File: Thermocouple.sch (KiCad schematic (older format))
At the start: 28 parts, among them P2 CONN_3X2, P3 CONN_2, U2 MCP3901, U3 LMT84, U4 OPA4170

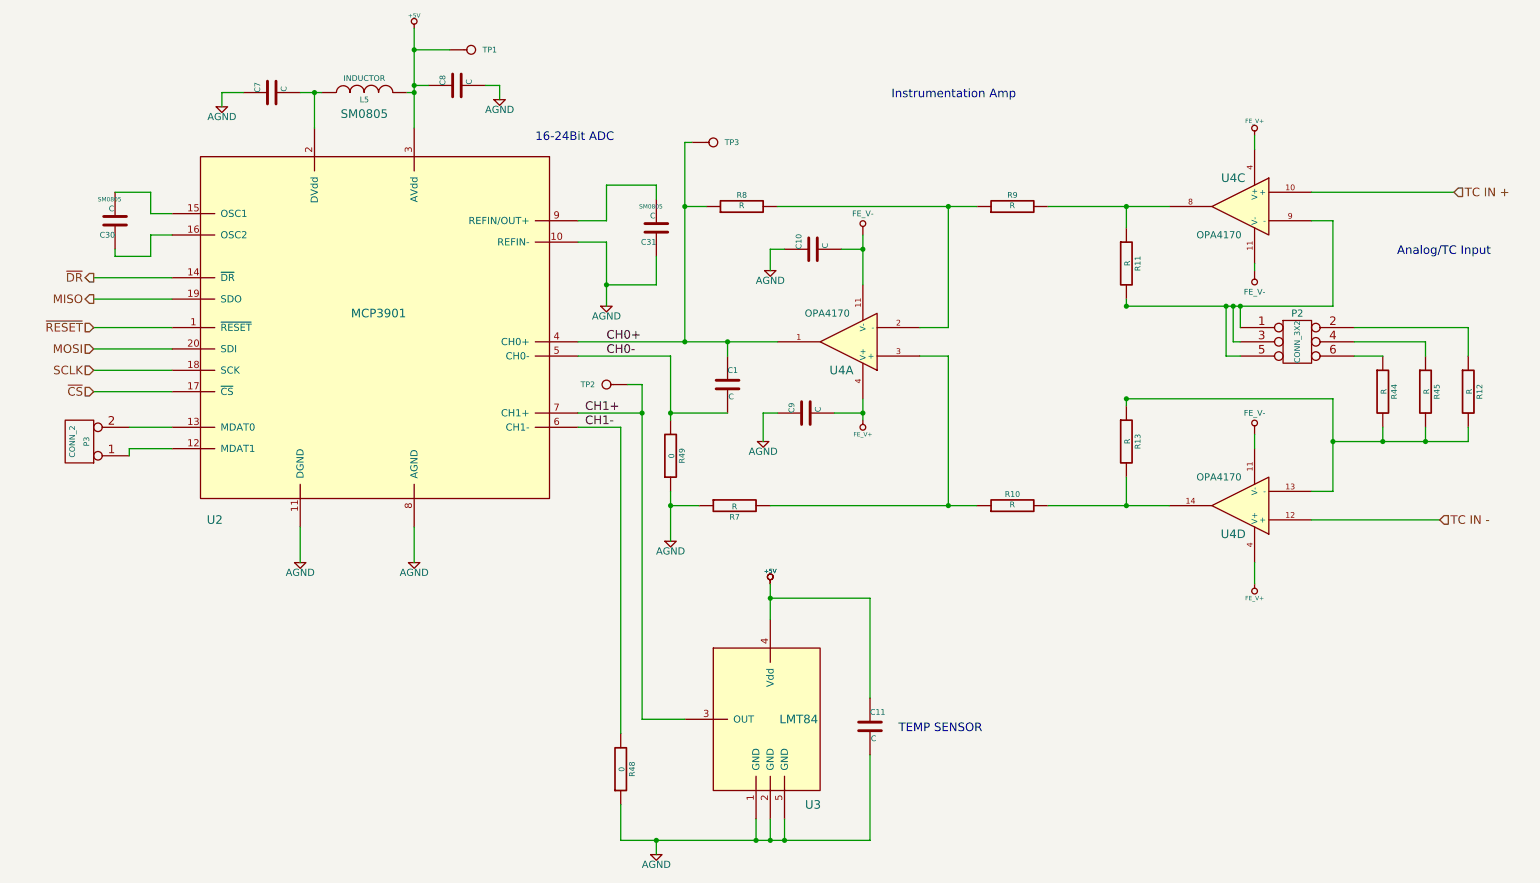
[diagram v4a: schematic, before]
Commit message: Analog IO Cleanup/Additions
Added some placed holder caps and resistors
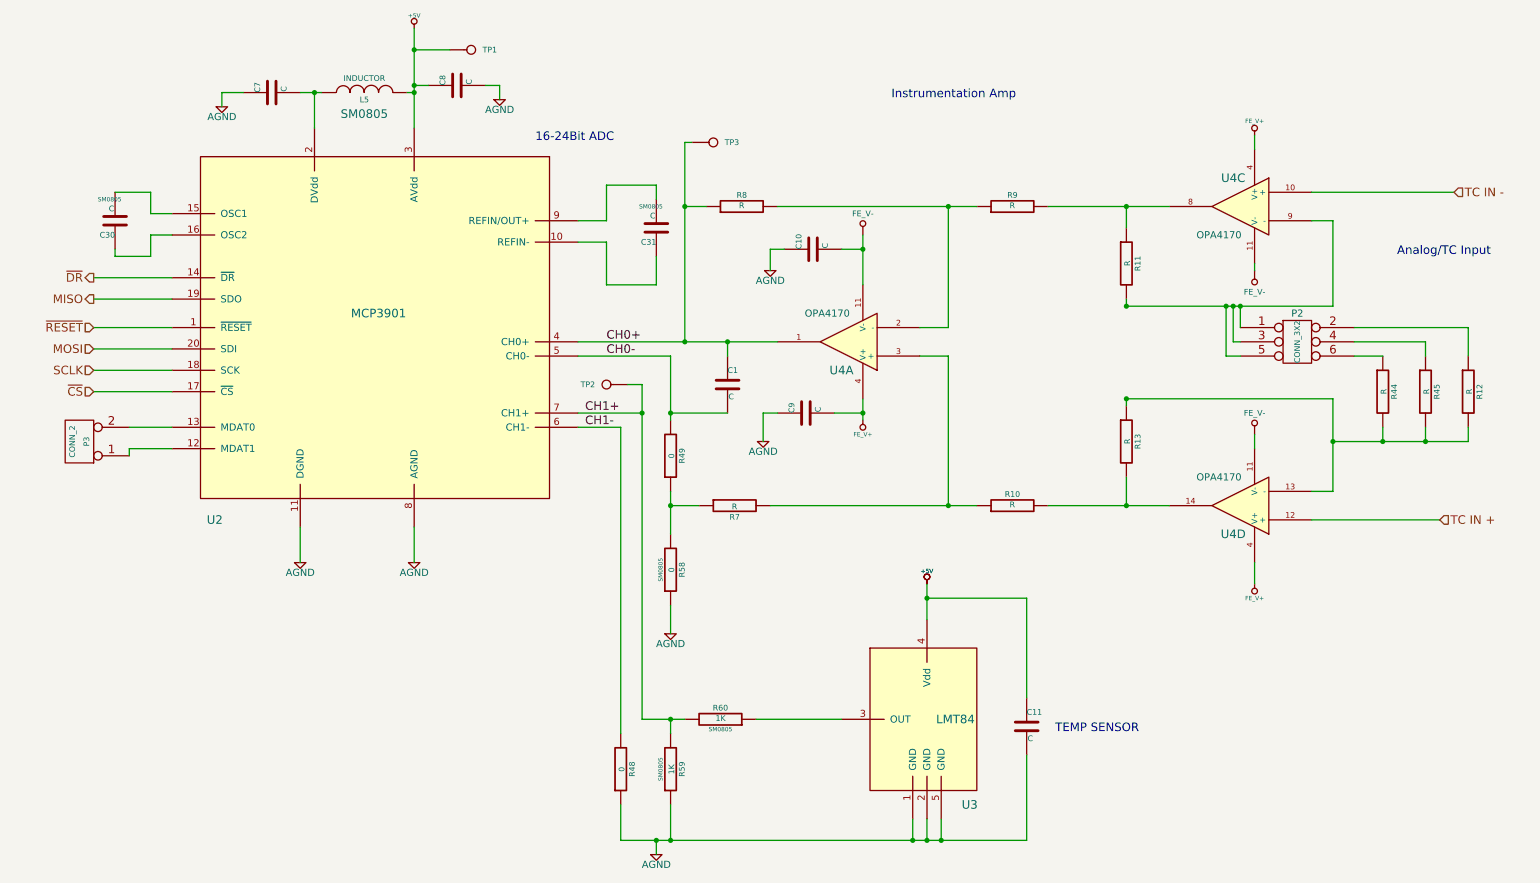
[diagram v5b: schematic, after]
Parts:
- added R58: 0, SM0805, symbol R
- added R59, R60: 1K, SM0805, symbol R
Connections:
- net AGND: now also R58.1, R59.1; no longer C31.1, R49.1, R7.1, U2.10 (REFIN-)
- net CH1+: now also R59.2, R60.2; no longer U3.3 (OUT)
- net TC IN +: now also U4.12 (+); no longer U4.10 (+)
- net TC IN -: now also U4.10 (+); no longer U4.12 (+)
- new net: R49.1, R58.2, R7.1
- new net: C31.1, U2.10 (REFIN-)
- new net: R60.1, U3.3 (OUT)
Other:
- moved on the sheet: C11, U3
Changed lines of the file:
@@
-EESchema Schematic File Version 2  date 12/18/2013 11:27:15 PM
+EESchema Schematic File Version 2  date 2/16/2014 3:41:32 PM
 LIBS:power
 LIBS:device
@@
 Sheet 2 9
 Title ""
-Date "19 dec 2013"
+Date "16 feb 2014"
 Rev ""
 Comp ""
@@
 $EndDescr
 Text HLabel 10400 2250 2    60   Input ~ 0
+TC IN -
+Text HLabel 10300 4550 2    60   Input ~ 0
 TC IN +
-Text HLabel 10300 4550 2    60   Input ~ 0
-TC IN -
 Text HLabel 850  3350 0    60   Input ~ 0
 MOSI
@@
 L LMT84 U3
 U 1 1 52579673
-P 5600 6100
-F 0 "U3" H 5900 5650 60  0000 C CNN
-F 1 "LMT84" H 5800 6250 60  0000 C CNN
-F 2 "" H 5700 6100 60  0000 C CNN
-F 3 "" H 5700 6100 60  0000 C CNN
-	1    5600 6100
-	1    0    0    -1
-$EndComp
-Wire Wire Line
-	4700 5950 5000 5950
+P 6700 6100
+F 0 "U3" H 7000 5650 60  0000 C CNN
+F 1 "LMT84" H 6900 6250 60  0000 C CNN
+F 2 "" H 6800 6100 60  0000 C CNN
+F 3 "" H 6800 6100 60  0000 C CNN
+	1    6700 6100
+	1    0    0    -1
+$EndComp
 Wire Wire Line
 	4700 3600 4700 5950
@@
 	4250 3900 4550 3900
 Wire Wire Line
-	4550 6800 6300 6800
-Wire Wire Line
-	5500 6800 5500 6650
-Wire Wire Line
-	5600 6800 5600 6650
-Connection ~ 5500 6800
-Wire Wire Line
-	5700 6800 5700 6650
-Connection ~ 5600 6800
+	4550 6800 7400 6800
+Wire Wire Line
+	6600 6800 6600 6650
+Wire Wire Line
+	6700 6800 6700 6650
+Connection ~ 6600 6800
+Wire Wire Line
+	6800 6800 6800 6650
+Connection ~ 6700 6800
 Wire Wire Line
 	4800 6900 4800 6800
 Connection ~ 4800 6800
 $Comp
-L +5V #PWR11
+L +5V #PWR01
 U 1 1 5257A1D1
-P 5600 5000
-F 0 "#PWR11" H 5600 5090 20  0001 C CNN
-F 1 "+5V" H 5600 5090 30  0000 C CNN
-F 2 "~" H 5600 5000 60  0000 C CNN
-F 3 "~" H 5600 5000 60  0000 C CNN
-	1    5600 5000
-	1    0    0    -1
-$EndComp
-Wire Wire Line
-	5600 5000 5600 5250
+P 6700 5000
+F 0 "#PWR01" H 6700 5090 20  0001 C CNN
+F 1 "+5V" H 6700 5090 30  0000 C CNN
+F 2 "~" H 6700 5000 60  0000 C CNN
+F 3 "~" H 6700 5000 60  0000 C CNN
+	1    6700 5000
+	1    0    0    -1
+$EndComp
+Wire Wire Line
+	6700 5000 6700 5250
 $Comp
 L C C11
 U 1 1 5257A1D8
-P 6300 6000
-F 0 "C11" H 6300 6100 40  0000 L CNN
-F 1 "C" H 6306 5915 40  0000 L CNN
-F 2 "~" H 6338 5850 30  0000 C CNN
-F 3 "~" H 6300 6000 60  0000 C CNN
-	1    6300 6000
-	1    0    0    -1
-$EndComp
-Wire Wire Line
-	6300 5800 6300 5100
-Wire Wire Line
-	6300 5100 5600 5100
-Connection ~ 5600 5100
-Wire Wire Line
-	6300 6800 6300 6200
-Connection ~ 5700 6800
+P 7400 6000
+F 0 "C11" H 7400 6100 40  0000 L CNN
+F 1 "C" H 7406 5915 40  0000 L CNN
+F 2 "~" H 7438 5850 30  0000 C CNN
+F 3 "~" H 7400 6000 60  0000 C CNN
+	1    7400 6000
+	1    0    0    -1
+$EndComp
+Wire Wire Line
+	7400 5800 7400 5100
+Wire Wire Line
+	7400 5100 6700 5100
+Connection ~ 6700 5100
+Wire Wire Line
+	7400 6800 7400 6200
+Connection ~ 6800 6800
 $Comp
 L C C9
@@
 	6050 3800 6250 3800
 $Comp
-L +5V #PWR12
+L +5V #PWR02
 U 1 1 5257A5A4
-P 5600 5000
-F 0 "#PWR12" H 5600 5090 20  0001 C CNN
-F 1 "+5V" H 5600 5090 30  0000 C CNN
-F 2 "~" H 5600 5000 60  0000 C CNN
-F 3 "~" H 5600 5000 60  0000 C CNN
-	1    5600 5000
-	1    0    0    -1
-$EndComp
-$Comp
-L +5V #PWR3
+P 6700 5000
+F 0 "#PWR02" H 6700 5090 20  0001 C CNN
+F 1 "+5V" H 6700 5090 30  0000 C CNN
+F 2 "~" H 6700 5000 60  0000 C CNN
+F 3 "~" H 6700 5000 60  0000 C CNN
+	1    6700 5000
+	1    0    0    -1
+$EndComp
+$Comp
+L +5V #PWR03
 U 1 1 5257A5AA
 P 3100 1100
-F 0 "#PWR3" H 3100 1190 20  0001 C CNN
+F 0 "#PWR03" H 3100 1190 20  0001 C CNN
 F 1 "+5V" H 3100 1190 30  0000 C CNN
 F 2 "~" H 3100 1100 60  0000 C CNN
@@
 Wire Wire Line
 	3100 4600 3100 4850
-Text Notes 6500 6050 0    60   ~ 0
+Text Notes 7600 6050 0    60   ~ 0
 TEMP SENSOR
 Text HLabel 850  3200 0    60   Input ~ 0
@@
 $EndComp
 Wire Wire Line
-	4900 4350 4900 4700
+	4900 4350 4900 4650
 $Comp
 L R R48
@@
 	4550 3900 4550 6050
 $Comp
-L FE_V- #PWR13
+L FE_V- #PWR11
 U 1 1 526E01DB
 P 6250 2550
-F 0 "#PWR13" H 6250 2750 40  0001 C CNN
+F 0 "#PWR11" H 6250 2750 40  0001 C CNN
 F 1 "FE_V-" H 6250 2700 40  0000 C CNN
 F 2 "~" H 6250 2550 60  0000 C CNN
@@
 $EndComp
 $Comp
-L FE_V+ #PWR14
+L FE_V+ #PWR04
 U 1 1 526E01E1
 P 6250 3850
-F 0 "#PWR14" H 6250 3950 30  0001 C CNN
+F 0 "#PWR04" H 6250 3950 30  0001 C CNN
 F 1 "FE_V+" H 6250 3950 30  0000 C CNN
 F 2 "~" H 6250 3850 60  0000 C CNN
@@
 $EndComp
 $Comp
-L FE_V+ #PWR18
+L FE_V+ #PWR05
 U 1 1 526E01F1
 P 9000 5000
-F 0 "#PWR18" H 9000 5100 30  0001 C CNN
+F 0 "#PWR05" H 9000 5100 30  0001 C CNN
 F 1 "FE_V+" H 9000 5100 30  0000 C CNN
 F 2 "~" H 9000 5000 60  0000 C CNN
@@
 $EndComp
 $Comp
-L FE_V+ #PWR15
+L FE_V+ #PWR06
 U 1 1 526E020D
 P 9000 1850
-F 0 "#PWR15" H 9000 1950 30  0001 C CNN
+F 0 "#PWR06" H 9000 1950 30  0001 C CNN
 F 1 "FE_V+" H 9000 1950 30  0000 C CNN
 F 2 "~" H 9000 1850 60  0000 C CNN
@@
 $EndComp
 $Comp
-L AGND #PWR4
+L AGND #PWR07
 U 1 1 527EEF67
 P 3100 4850
-F 0 "#PWR4" H 3100 4850 40  0001 C CNN
+F 0 "#PWR07" H 3100 4850 40  0001 C CNN
 F 1 "AGND" H 3100 4780 50  0000 C CNN
 F 2 "~" H 3100 4850 60  0000 C CNN
@@
 $EndComp
 $Comp
-L AGND #PWR2
+L AGND #PWR08
 U 1 1 527EEF6D
 P 2300 4850
-F 0 "#PWR2" H 2300 4850 40  0001 C CNN
+F 0 "#PWR08" H 2300 4850 40  0001 C CNN
 F 1 "AGND" H 2300 4780 50  0000 C CNN
 F 2 "~" H 2300 4850 60  0000 C CNN
@@
 $EndComp
 $Comp
-L AGND #PWR1
+L AGND #PWR09
 U 1 1 527EEF73
 P 1750 1650
-F 0 "#PWR1" H 1750 1650 40  0001 C CNN
+F 0 "#PWR09" H 1750 1650 40  0001 C CNN
 F 1 "AGND" H 1750 1580 50  0000 C CNN
 F 2 "~" H 1750 1650 60  0000 C CNN
@@
 $EndComp
 $Comp
-L AGND #PWR5
+L AGND #PWR010
 U 1 1 527EEF79
 P 3700 1600
-F 0 "#PWR5" H 3700 1600 40  0001 C CNN
+F 0 "#PWR010" H 3700 1600 40  0001 C CNN
 F 1 "AGND" H 3700 1530 50  0000 C CNN
 F 2 "~" H 3700 1600 60  0000 C CNN
@@
 $EndComp
 $Comp
-L AGND #PWR10
+L AGND #PWR011
 U 1 1 527EEF7F
 P 5600 2800
-F 0 "#PWR10" H 5600 2800 40  0001 C CNN
+F 0 "#PWR011" H 5600 2800 40  0001 C CNN
 F 1 "AGND" H 5600 2730 50  0000 C CNN
 F 2 "~" H 5600 2800 60  0000 C CNN
@@
 $EndComp
 $Comp
-L AGND #PWR9
+L AGND #PWR012
 U 1 1 527EEF85
 P 5550 4000
-F 0 "#PWR9" H 5550 4000 40  0001 C CNN
+F 0 "#PWR012" H 5550 4000 40  0001 C CNN
 F 1 "AGND" H 5550 3930 50  0000 C CNN
 F 2 "~" H 5550 4000 60  0000 C CNN
@@
 $EndComp
 $Comp
-L AGND #PWR8
+L AGND #PWR013
 U 1 1 527EEF8B
-P 4900 4700
-F 0 "#PWR8" H 4900 4700 40  0001 C CNN
-F 1 "AGND" H 4900 4630 50  0000 C CNN
-F 2 "~" H 4900 4700 60  0000 C CNN
-F 3 "~" H 4900 4700 60  0000 C CNN
-	1    4900 4700
-	1    0    0    -1
-$EndComp
-$Comp
-L AGND #PWR7
+P 4900 5350
+F 0 "#PWR013" H 4900 5350 40  0001 C CNN
+F 1 "AGND" H 4900 5280 50  0000 C CNN
+F 2 "~" H 4900 5350 60  0000 C CNN
+F 3 "~" H 4900 5350 60  0000 C CNN
+	1    4900 5350
+	1    0    0    -1
+$EndComp
+$Comp
+L AGND #PWR014
 U 1 1 527EEF91
 P 4800 6900
-F 0 "#PWR7" H 4800 6900 40  0001 C CNN
+F 0 "#PWR014" H 4800 6900 40  0001 C CNN
 F 1 "AGND" H 4800 6830 50  0000 C CNN
 F 2 "~" H 4800 6900 60  0000 C CNN
@@
 	4450 2200 4450 2450
 Wire Wire Line
-	4450 2600 4450 3050
-Wire Wire Line
 	4450 2900 4800 2900
 Wire Wire Line
 	4800 2900 4800 2700
-$Comp
-L AGND #PWR6
-U 1 1 529271FF
-P 4450 3050
-F 0 "#PWR6" H 4450 3050 40  0001 C CNN
-F 1 "AGND" H 4450 2980 50  0000 C CNN
-F 2 "~" H 4450 3050 60  0000 C CNN
-F 3 "~" H 4450 3050 60  0000 C CNN
-	1    4450 3050
-	1    0    0    -1
-$EndComp
-Connection ~ 4450 2900
 $Comp
 L CONN_1 TP3
@@
 	3100 1250 3350 1250
 Connection ~ 3100 1250
+$Comp
+L R R58
+U 1 1 53010C4F
+P 4900 4900
+F 0 "R58" V 4980 4900 40  0000 C CNN
+F 1 "0" V 4907 4901 40  0000 C CNN
+F 2 "SM0805" V 4830 4900 30  0000 C CNN
+F 3 "~" H 4900 4900 30  0000 C CNN
+	1    4900 4900
+	1    0    0    1
+$EndComp
+Wire Wire Line
+	4900 5150 4900 5350
+$Comp
+L R R60
+U 1 1 53010D95
+P 5250 5950
+F 0 "R60" V 5330 5950 40  0000 C CNN
+F 1 "1K" V 5257 5951 40  0000 C CNN
+F 2 "SM0805" V 5180 5950 30  0000 C CNN
+F 3 "~" H 5250 5950 30  0000 C CNN
+	1    5250 5950
+	0    1    -1   0
+$EndComp
+Wire Wire Line
+	6100 5950 5500 5950
+Wire Wire Line
+	4700 5950 5000 5950
+$Comp
+L R R59
+U 1 1 53010EB2
+P 4900 6300
+F 0 "R59" V 4980 6300 40  0000 C CNN
+F 1 "1K" V 4907 6301 40  0000 C CNN
+F 2 "SM0805" V 4830 6300 30  0000 C CNN
+F 3 "~" H 4900 6300 30  0000 C CNN
+	1    4900 6300
+	1    0    0    1
+$EndComp
+Wire Wire Line
+	4900 5950 4900 6050
+Connection ~ 4900 5950
+Wire Wire Line
+	4900 6550 4900 6800
+Connection ~ 4900 6800
+Wire Wire Line
+	4450 2600 4450 2900
 $EndSCHEMATC

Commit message: Added Passive Values and SPICE models
As part of week 1 of Session 1B, we added a SPICE model of the In amp
and went through and assigned values to all of the passive components.
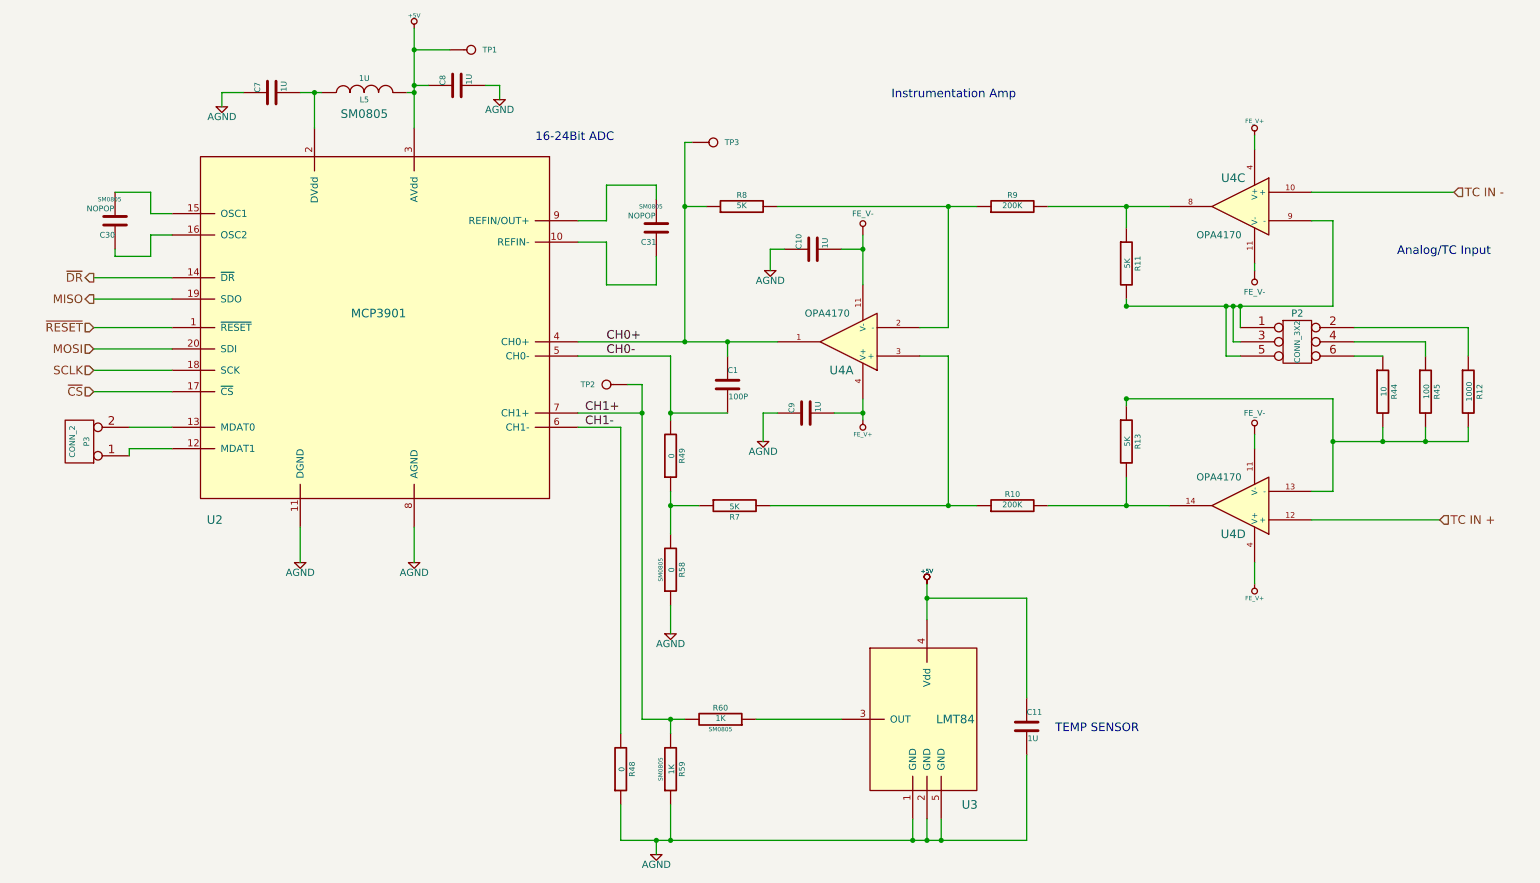
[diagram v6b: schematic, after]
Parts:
- C1: value C -> 100P
- C10, C11, C7, C8, C9: value C -> 1U
- C30, C31: value C -> NOPOP
- L5: value INDUCTOR -> 1U
- R10, R9: value R -> 200K
- R11, R13, R7, R8: value R -> 5K
- R12: value R -> 1000
- R44: value R -> 10
- R45: value R -> 100
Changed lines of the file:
@@
-EESchema Schematic File Version 2  date 2/16/2014 3:41:32 PM
+EESchema Schematic File Version 2  date 4/16/2014 11:04:06 PM
 LIBS:power
 LIBS:device
@@
 Sheet 2 9
 Title ""
-Date "16 feb 2014"
+Date "17 apr 2014"
 Rev ""
 Comp ""
@@
 P 5300 3600
 F 0 "C1" H 5300 3700 40  0000 L CNN
-F 1 "C" H 5306 3515 40  0000 L CNN
+F 1 "100P" H 5306 3515 40  0000 L CNN
 F 2 "~" H 5338 3450 30  0000 C CNN
 F 3 "~" H 5300 3600 60  0000 C CNN
@@
 P 8100 2750
 F 0 "R11" V 8180 2750 40  0000 C CNN
-F 1 "R" V 8107 2751 40  0000 C CNN
+F 1 "5K" V 8107 2751 40  0000 C CNN
 F 2 "~" V 8030 2750 30  0000 C CNN
 F 3 "~" H 8100 2750 30  0000 C CNN
@@
 P 10500 3650
 F 0 "R12" V 10580 3650 40  0000 C CNN
-F 1 "R" V 10507 3651 40  0000 C CNN
+F 1 "1000" V 10507 3651 40  0000 C CNN
 F 2 "~" V 10430 3650 30  0000 C CNN
 F 3 "~" H 10500 3650 30  0000 C CNN
@@
 P 8100 4000
 F 0 "R13" V 8180 4000 40  0000 C CNN
-F 1 "R" V 8107 4001 40  0000 C CNN
+F 1 "5K" V 8107 4001 40  0000 C CNN
 F 2 "~" V 8030 4000 30  0000 C CNN
 F 3 "~" H 8100 4000 30  0000 C CNN
@@
 P 7300 2350
 F 0 "R9" V 7380 2350 40  0000 C CNN
-F 1 "R" V 7307 2351 40  0000 C CNN
+F 1 "200K" V 7307 2351 40  0000 C CNN
 F 2 "~" V 7230 2350 30  0000 C CNN
 F 3 "~" H 7300 2350 30  0000 C CNN
@@
 P 5400 2350
 F 0 "R8" V 5480 2350 40  0000 C CNN
-F 1 "R" V 5407 2351 40  0000 C CNN
+F 1 "5K" V 5407 2351 40  0000 C CNN
 F 2 "~" V 5330 2350 30  0000 C CNN
 F 3 "~" H 5400 2350 30  0000 C CNN
@@
 P 5350 4450
 F 0 "R7" V 5430 4450 40  0000 C CNN
-F 1 "R" V 5357 4451 40  0000 C CNN
+F 1 "5K" V 5357 4451 40  0000 C CNN
 F 2 "~" V 5280 4450 30  0000 C CNN
 F 3 "~" H 5350 4450 30  0000 C CNN
@@
 P 7300 4450
 F 0 "R10" V 7380 4450 40  0000 C CNN
-F 1 "R" V 7307 4451 40  0000 C CNN
+F 1 "200K" V 7307 4451 40  0000 C CNN
 F 2 "~" V 7230 4450 30  0000 C CNN
 F 3 "~" H 7300 4450 30  0000 C CNN
@@
 P 9900 3650
 F 0 "R44" V 9980 3650 40  0000 C CNN
-F 1 "R" V 9907 3651 40  0000 C CNN
+F 1 "10" V 9907 3651 40  0000 C CNN
 F 2 "~" V 9830 3650 30  0000 C CNN
 F 3 "~" H 9900 3650 30  0000 C CNN
@@
 P 10200 3650
 F 0 "R45" V 10280 3650 40  0000 C CNN
-F 1 "R" V 10207 3651 40  0000 C CNN
+F 1 "100" V 10207 3651 40  0000 C CNN
 F 2 "~" V 10130 3650 30  0000 C CNN
 F 3 "~" H 10200 3650 30  0000 C CNN
@@
 P 7400 6000
 F 0 "C11" H 7400 6100 40  0000 L CNN
-F 1 "C" H 7406 5915 40  0000 L CNN
+F 1 "1U" H 7406 5915 40  0000 L CNN
 F 2 "~" H 7438 5850 30  0000 C CNN
 F 3 "~" H 7400 6000 60  0000 C CNN
@@
 P 5850 3800
 F 0 "C9" H 5850 3900 40  0000 L CNN
-F 1 "C" H 5856 3715 40  0000 L CNN
+F 1 "1U" H 5856 3715 40  0000 L CNN
 F 2 "~" H 5888 3650 30  0000 C CNN
 F 3 "~" H 5850 3800 60  0000 C CNN
@@
 P 5900 2650
 F 0 "C10" H 5900 2750 40  0000 L CNN
-F 1 "C" H 5906 2565 40  0000 L CNN
+F 1 "1U" H 5906 2565 40  0000 L CNN
 F 2 "~" H 5938 2500 30  0000 C CNN
 F 3 "~" H 5900 2650 60  0000 C CNN
@@
 P 3400 1500
 F 0 "C8" H 3400 1600 40  0000 L CNN
-F 1 "C" H 3406 1415 40  0000 L CNN
+F 1 "1U" H 3406 1415 40  0000 L CNN
 F 2 "~" H 3438 1350 30  0000 C CNN
 F 3 "~" H 3400 1500 60  0000 C CNN
@@
 P 2100 1550
 F 0 "C7" H 2100 1650 40  0000 L CNN
-F 1 "C" H 2106 1465 40  0000 L CNN
+F 1 "1U" H 2106 1465 40  0000 L CNN
 F 2 "~" H 2138 1400 30  0000 C CNN
 F 3 "~" H 2100 1550 60  0000 C CNN
@@
 P 2750 1550
 F 0 "L5" V 2700 1550 40  0000 C CNN
-F 1 "INDUCTOR" V 2850 1550 40  0000 C CNN
+F 1 "1U" V 2850 1550 40  0000 C CNN
 F 2 "SM0805" V 2600 1550 60  0000 C CNN
 F 3 "~" H 2750 1550 60  0000 C CNN
@@
 P 1000 2450
 F 0 "C30" H 1000 2550 40  0000 L CNN
-F 1 "C" H 1006 2365 40  0000 L CNN
+F 1 "NOPOP" H 1006 2365 40  0000 L CNN
 F 2 "SM0805" H 1038 2300 30  0000 C CNN
 F 3 "~" H 1000 2450 60  0000 C CNN
@@
 P 4800 2500
 F 0 "C31" H 4800 2600 40  0000 L CNN
-F 1 "C" H 4806 2415 40  0000 L CNN
+F 1 "NOPOP" H 4806 2415 40  0000 L CNN
 F 2 "SM0805" H 4838 2350 30  0000 C CNN
 F 3 "~" H 4800 2500 60  0000 C CNN
